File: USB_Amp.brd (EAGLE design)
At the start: 80 x 72 mm, 140 parts, among them CON1 USB-C, CON2 PROG, CON3 DC IN, CON4 VOLUEME, CON5 SWD, IC1 3.3V, IC2 PIC32MZEF, IC3 SSM3582, IC4 +5V, IC5 1.8V, IC6 TL431, IC7 STM32G031F, IC8 +5V, IC9 3.3V, Q1 NPN, Q2 NPN, X1 24.576MHz, X2 22.5792MHz, X3 12MHz

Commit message: 取り合えず
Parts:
- removed CON4: VOLUEME, my_connector:VOL_CON
- removed FB4: FB, my_rcl:1608-J
- removed FB5, FB6, FB7, FB8: FB, my_rcl:2012-FB
- removed JP1: IO, my_connector:1X05
- removed L3, L4: 15uH, my_rcl:L5-7,5
- removed X2: 22.5792MHz, my_rcl:KC3225
- added C65: 0.1u, my_rcl:1005
- added C66, C67: 470u, my_rcl:E5-10
- added C68, C69, C70, C71: 1u, my_rcl:2012
- added C72: 1u, my_rcl:1608C
- added C73, C77, C78, C79, C80: 100p, my_rcl:1608C
- added C74, C75, C76: 4.7u, my_rcl:3216
- added CON6: USB-C, my_connector:5077CR-16-SMC2-BK-TR
- added D6: 1mA, my_rcl:SOD123
- added D7: FAULT, my_rcl:D1608
- added D8: LED2, my_rcl:D1608
- added FB13: FB, my_rcl:3216-FB
- added HT1: HEATSINK-5, my_connector:V2199N1
- added Q3: PNP, my_ic:SC59
- added R27, R34, R35: 1k, my_rcl:1608
- added R28: DNP, my_rcl:1608
- added R29: 1k, my_rcl:2012
- added R30: 100k, my_rcl:1608
- added R31, R32: 5.1k, my_rcl:1608
- added R33, R36, R37: 3.3k, my_rcl:1608
- added R38, R39, R40, R41: 22, my_rcl:1608
- C14, C15: value 22p -> 10p
- C16, C17, C18, C19: value 0.22u -> 1u
- C20: value 10n -> 2.2u; device my_rcl:1005 -> my_rcl:1608C
- C21: value 10n -> 1u; device my_rcl:1005 -> my_rcl:2012
- C22, C23: value 0.1u -> 1u; device my_rcl:1608C -> my_rcl:2012
- C24, C25: device my_rcl:1005 -> my_rcl:3225-3
- C26, C40: value 10u -> 0.1u; device my_rcl:2012 -> my_rcl:3225-3
- C27: value 10u -> 0.47uF; device my_rcl:2012 -> my_rcl:C050W
- C29, C44: value 100p -> 0.47uF; device my_rcl:1608-2 -> my_rcl:C050W
- C31: value 0.1u -> 100p; device my_rcl:1608C -> my_rcl:1608-2
- C34: value 0.1u -> 10n; device my_rcl:C050W -> my_rcl:1005
- C35: value 0.1u -> 100p; device my_rcl:C050W -> my_rcl:1608-2
- C36, C37, C51: value 0.47uF -> 100p; device my_rcl:C050W -> my_rcl:1608-2
- C38: value 47u -> DNP; device my_rcl:E2.5-5 -> my_rcl:1608C
- C39: value 0.1u -> 10u; device my_rcl:1608C -> my_rcl:3216
- C41, C55: value DNP -> 10n; device my_rcl:1608-2 -> my_rcl:1005
- C42: value DNP -> 0.1u; device my_rcl:1608-2 -> my_rcl:1608C
- C45, C46: value 100p -> 0.1u; device my_rcl:1608-2 -> my_rcl:1608C
- C47: value 100p -> 10n; device my_rcl:1608-2 -> my_rcl:1005
- C48: device my_rcl:C050W -> my_rcl:1608C
- C49: value 0.1u -> 1u; device my_rcl:C050W -> my_rcl:1608C
- C50: value 0.47uF -> 0.1u; device my_rcl:C050W -> my_rcl:1608C
- C54: value DNP -> 10u; device my_rcl:1608-2 -> my_rcl:3216
- C56: value 1000u -> 470u; device my_rcl:E5-13 -> my_rcl:E5-10
- C59: value DNP -> 0.47uF; device my_rcl:1608C -> my_rcl:C050W
- C62: value 220u -> 1u; device my_rcl:E2,5-8 -> my_rcl:1608C
- C7: value 22u -> 1u; device my_rcl:3225 -> my_rcl:1608C
- CON3: value DC IN -> PWR IN
- D1: value SBD -> D; device my_rcl:SOD523 -> my_rcl:SOD323
- D4: value 5.6mA -> D; device my_rcl:SOD123 -> my_rcl:SOD323
- FB1, FB2: device my_rcl:1608-J -> my_rcl:1608-FB
- FB3: device my_rcl:1608-J -> my_rcl:2012-R
- IC3: value SSM3582 -> TAS6422; device my_ic:QFN40HT -> my_ic:HSSOP56-F
- IC4: value +5V -> 3.3V; device my_ic:TO220-SOP-DUAL -> my_ic:SOT23-5
- IC5: value 1.8V -> 3.3V
- IC6: device my_ic:SOT89 -> my_ic:TO220-SOP-DUAL
- IC7: value STM32G031F -> STM32G030F
- IC8: value +5V -> 7805
- IC9: value 3.3V -> CH221; device my_ic:SOT23-5 -> my_ic:SOT23-6
- L1, L2: value 15uH -> 10uH; device my_rcl:L5-7,5 -> my_rcl:UA8014
- R1: value 10k -> 5.1
- R10, R11, R12: device my_rcl:1608-J -> my_rcl:1005
- R13: value LRCLK -> 10; device my_rcl:1608-J -> my_rcl:3216-3
- R14: value DATA -> 10; device my_rcl:1608-J -> my_rcl:3216-3
- R15: value SCK -> 39; device my_rcl:1608-J -> my_rcl:1608
- R16: value 10 -> 100; device my_rcl:2012 -> my_rcl:1608
- R17: value 10 -> 50k; device my_rcl:2012 -> my_rcl:RK0972
- R19, R20: device my_rcl:2012 -> my_rcl:3216-3
- R23: value 10k -> 3.3k
- R3: value 10k -> 10; device my_rcl:1608 -> my_rcl:2012-R
- R6: value 1k -> 10k
- R7: value 1k -> 3.3k
- R8: value 10k -> 10
- R9: value 10k -> 39
- TP1, TP2: device my_connector:TESTPIN-BIG -> my_connector:TESTPIN-LARGE
- TP3: value R_P -> R_N; device my_connector:TESTPIN-BIG -> my_connector:TESTPIN-LARGE
- TP4: value R_N -> R_P; device my_connector:TESTPIN-BIG -> my_connector:TESTPIN-LARGE
- X3: device my_rcl:KC3225-2 -> my_rcl:KC3225-CRYSTAL
- moved R17 73.1 mm to (90.0, 46.0), flipped to the top
- moved IC5 71.9 mm to (78.8, 36.5)
- moved C59 68.3 mm to (10.0, 24.5), turned to 270 degrees
- moved C30 61.5 mm to (65.5, 34.0), turned to 90 degrees
- moved C48 60.6 mm to (55.5, 21.8), turned to 270 degrees
- moved R16 60.6 mm to (59.2, 55.2)
- moved C46 57.9 mm to (51.2, 18.8)
- moved IC4 57.3 mm to (62.0, 34.0), turned to 90 degrees
- moved C47 55.0 mm to (51.8, 20.2)
- moved TP4 54.3 mm to (3.25, 17.8)
- moved FB3 54.0 mm to (58.0, 26.8), turned to 270 degrees
- moved C50 53.4 mm to (68.5, 49.2), flipped to the bottom, turned to 90 degrees
- moved TP3 52.1 mm to (3.25, 22.2)
- moved C54 51.4 mm to (67.8, 34.5), turned to 90 degrees
- moved C39 50.5 mm to (53.8, 47.5), flipped to the bottom, turned to 90 degrees
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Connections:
- removed net +12V: C20.1, C21.1, C24.1, C25.1, C26.1, C27.1, C52.+, C53.+, C56.+, IC3.14, IC3.15, IC3.16, IC3.17, IC3.34, IC3.35, IC3.36, IC3.37, Q2.3, R18.2, R21.2
- removed net AMP_AVDD: C23.1, C38.+, C40.1, IC3.24, IC4.3, IC4.6
- removed net EN_44.1K: IC2.29, R9.2, X2.1
- removed net EN_48K: IC2.28, R8.2, X1.1
- removed net MCLK: IC2.22, X1.3, X2.3
- removed net STM_IO16: IC7.16, JP1.2
- removed net STM_IO17: IC7.17, JP1.3
- removed net STM_IO20: IC7.20, JP1.4
- new net AMP_FAULT: IC3.26, IC3.27, R33.2
- new net AMP_MUTE: IC3.25, R35.1
- new net AMP_STANBY: IC3.24, R34.1
- new net I2S_MCLK: IC3.12, R9.2
- new net LED2: IC2.45, R37.2
- new net N$25: C26.1, R13.1
- new net N$26: FB2.2, R8.1
- new net N$27: R15.1, R9.1, X1.3
- new net N$28: FB3.1, R3.2
- new net N$29: Q3.2, R16.1
- new net N$32: CON6.B5:CC2, IC9.5, R32.1
- new net N$33: C49.1, IC9.1, R29.1, R30.2
- new net N$34: IC9.6, R30.1
- new net N$35: D7.K, R33.1
- new net N$37: D1.1, D4.2
- new net N$38: D1.2, D6.1, Q3.1
- new net N$39: IC7.16, R35.2
- new net N$42: IC7.17, R34.2
- new net N$44: D8.A, R37.1
- new net N$45: C77.1, R38.1
- new net N$46: C78.2, R39.2
- new net N$47: C79.2, R40.2
- new net N$48: C80.1, R41.1
- new net N$6: C19.2, IC3.31
- new net PIC_MCLK: IC2.58, R15.2
- new net PVDD: C34.1, C39.1, C41.1, C42.1, C45.1, C46.1, C47.1, C52.+, C53.+, C56.+, C66.+, C68.1, C69.1, C70.1, C74.1, C75.1, C76.1, IC3.2, IC3.29, IC3.30, IC3.42, IC3.43, Q2.3, R18.2, R21.2, R3.1
- new net VBAT: C48.1, C55.1, C67.+, C71.1, FB3.2, IC3.3
- new net VINC_+: CON6.A4,B9:VBUS, CON6.B4,A9:VBUS, FB13.1, R29.2
- net +3V3: now also IC5.5, R17.1, R17.4, R28.2; no longer CON4.1, IC9.5, JP1.1
- net +3V3D: now also C6.1; no longer FB2.1
- net +5V: now also C30.1, C54.1, IC4.1, IC4.3, IC5.1, IC5.3; no longer C62.+, FB3.1, IC9.1, IC9.3
- net AMP_DVDD: now also C62.1, C65.1, C72.1, D7.A, FB2.1, IC3.19, IC4.5; no longer C22.1, IC3.28, IC5.5
- net AMP_OUTN_L: now also C19.1, R40.1; no longer C18.1, C41.2, FB5.2, IC3.33
- net AMP_OUTN_R: now also C17.1, IC3.38, L2.3, R38.2; no longer C19.2, C54.2, FB7.2, IC3.18, IC3.19, L3.2
- net AMP_OUTP_L: now also C18.2, IC3.34, L1.4, R41.2; no longer C16.1, C42.1, FB6.1, IC3.38, IC3.39, L2.2
- net AMP_OUTP_R: now also C16.2, IC3.40, L2.2, R39.1; no longer C17.2, C55.1, FB8.1, IC3.12, IC3.13, L4.1
- net EN_DDC: now also IC1.3, R6.1; no longer R1.1, R3.2
- net GND: now also C24.1, C25.1, C27.1, C27.3, C28.2, C29.1, C29.3, C34.2, C35.1, C36.2, C41.2, C44.3, C46.2, C48.2, C50.2, C54.2, C59.1, C59.3, C62.2, C65.2, C66.-, C67.-, C68.2, C69.2, C70.2, C71.2, C72.2, C73.2, C74.2, C75.2, C76.2, C77.2, C78.1, C79.1, C80.2, CON6.A1,B12:GND, CON6.B1,A12:GND, CON6.SHILED1, CON6.SHILED2, CON6.SHILED3, CON6.SHILED4, CON6.SHILED5, CON6.SHILED6, CON6.SHILED7, CON6.SHILED8, D6.2, D8.K, HT1.HT1, HT1.HT2, IC2.HT2, IC3.11, IC3.16, IC3.17, IC3.18, IC3.28, IC3.33, IC3.36, IC3.39, IC3.46, IC6.5, R17.3, R17.6, R31.2, R32.2, R6.2, R7.1; no longer C21.2, C22.2, C23.2, C24.2, C25.2, C27.2, C28.1, C29.2, C34.1, C34.3, C35.2, C35.4, C36.1, C36.3, C37.3, C38.-, C39.2, C41.1, C46.1, C48.1, C48.3, C49.4, C50.1, C50.3, C51.3, C54.1, C59.2, C62.-, CON4.3, D2.K, IC3.10, IC3.2, IC3.21, IC3.25, IC3.26, IC3.27, IC3.29, IC3.3, IC3.30, IC3.9, IC3.HT, IC3.HT1, IC3.HT2, IC3.HT3, IC3.HT4, IC4.5, JP1.5, R3.1, R8.1, R9.1, X2.2
- net I2C_SCL: now also IC3.20; no longer IC3.4
- net I2C_SDA: now also IC3.21; no longer IC3.5
- net I2S_DATA: now also IC3.15; no longer R14.1
- net I2S_LRCLK: now also IC3.14; no longer R13.1
- net I2S_SCK: now also IC3.13; no longer R15.1
- net LED0: now also D2.A, IC7.3; no longer IC2.2, R6.2
- net LED1: now also IC2.46, R36.2; no longer IC2.3, R7.2
- net N$10: now also C20.1, IC3.9; no longer IC3.6, R13.2
- net N$11: now also C21.2, IC3.8; no longer IC3.7, R14.2
- net N$12: now also C21.1, IC3.7; no longer C18.2, IC3.31
- net N$13: now also C22.1, C23.1, IC3.4; no longer C16.2, IC3.40
- net N$14: now also C18.1, IC3.35; no longer IC3.8, R15.2
- net N$15: now also C22.2, IC3.6; no longer C39.1, IC5.4
- net N$17: now also C17.2, IC3.37; no longer C17.1, IC3.11
- net N$18: now also C23.2, IC3.5; no longer C19.1, IC3.20
- net N$19: now also C16.1, IC3.41; no longer C30.1, FB3.2, IC5.1, IC5.3
- net N$20: now also C38.2, IC6.4, R27.1; no longer R21.1, R22.2
- net N$21: now also C24.2, R19.2; no longer C34.2, C34.4, R16.2
- net N$22: now also C40.1, R20.1; no longer C35.1, C35.3, R17.1
- net N$23: now also C38.1, IC6.6, Q3.3; no longer D4.2
- net N$24: now also C25.2, R14.2; no longer C31.1, FB4.2, IC4.1, IC4.4
- net N$3: now also FB1.2, R1.1; no longer CON1.A4,B9:VBUS, CON1.B4,A9:VBUS, FB1.1
- net N$30: now also C39.2, R21.1, R22.2, R27.2; no longer C48.2, C48.4, R19.2
- net N$31: now also CON6.A5:CC1, IC9.4, R31.1; no longer C49.1, C49.3, R20.1
- net N$4: now also C1.1, C2.1, IC1.1; no longer D1.A, IC1.3
- net N$72: now also C73.1, R17.2, R17.5, R28.1; no longer C59.1, CON4.2
- net N$8: now also D2.K, R7.2; no longer D2.A, R6.1
- net N$9: now also R36.1; no longer R7.1
- net PIC_COM1: now also IC2.44, IC7.15; no longer IC2.62, IC7.12
- net PIC_COM2: now also IC2.43, IC7.14; no longer IC2.64, IC7.13
- net PIC_COM3: now also IC2.42, IC7.13; no longer IC2.63, IC7.14
- net SP_OUTN_L: now also C27.2, C27.4, C35.2, C37.2, R19.1; no longer C28.2, C32.2, C36.2, C36.4, FB5.1, R16.1
- net SP_OUTN_R: now also C31.1, C33.1, C59.2, C59.4, L2.4, R13.2, TP3.1; no longer C44.2, C46.2, C50.2, C50.4, FB7.1, L3.1, R19.1, TP4.1
- net SP_OUTP_L: now also C28.1, C36.1, C44.2, C44.4, L1.3, R20.2; no longer C29.1, C33.1, C37.2, C37.4, FB6.2, L2.1, R17.2
- net SP_OUTP_R: now also C29.2, C29.4, C32.2, L2.1, R14.1, TP4.1; no longer C45.1, C47.1, C51.4, FB8.2, L4.2, R20.2, TP3.1
- net USB_VBUS: now also CON1.A4,B9:VBUS, CON1.B4,A9:VBUS, FB1.1; no longer C1.1, C2.1, D1.K, FB1.2, IC1.1
- net V+: now also C50.1, FB13.2, R16.2; no longer FB4.1
- net XVCC: now also R8.2, X1.1; no longer C6.1, FB2.2, X2.4
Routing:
- net +5V: track 97.1 -> 25.6 mm
- net V+: track 68.4 -> 10.0 mm, vias 0 -> 2
- net +12V: track 51.8 -> 0.00 mm, vias 12 -> 0
- net AMP_MUTE: track 0.00 -> 38.6 mm, vias 0 -> 2
- net AMP_STANBY: track 0.00 -> 38.6 mm, vias 0 -> 2
- net VBAT: track 0.00 -> 31.8 mm, vias 0 -> 2
- net PIC_MCLK: track 0.00 -> 26.0 mm
- net +3V3D: track 32.3 -> 58.3 mm, vias 12 -> 9
- net UART_TX: track 26.9 -> 3.77 mm, vias 1 -> 0
- net SP_OUTP_R: track 22.6 -> 0.00 mm, vias 0 -> 2
- net SP_OUTN_R: track 22.5 -> 0.00 mm, vias 0 -> 2
- net SP_OUTP_L: track 22.3 -> 0.00 mm, vias 0 -> 2
- net SP_OUTN_L: track 22.2 -> 0.00 mm, vias 0 -> 2
- net EN_DDC: track 9.84 -> 31.8 mm, vias 0 -> 2
- net STM_IO20: track 21.5 -> 0.00 mm
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- added copper zone on layer 16, net AMP_OUTN_L
- added copper zone on layer 16, net AMP_OUTN_R
- added copper zone on layer 16, net AMP_OUTP_L
- added copper zone on layer 16, net AMP_OUTP_R
- added copper zone on layer 1, net PVDD
- added copper zone on layer 16, net PVDD
- added copper zone on layer 1, net SP_OUTN_L
- added copper zone on layer 16, net SP_OUTN_L
- added copper zone on layer 1, net SP_OUTN_R
- added copper zone on layer 16, net SP_OUTN_R
- added copper zone on layer 1, net SP_OUTP_L
- added copper zone on layer 16, net SP_OUTP_L
- added copper zone on layer 1, net SP_OUTP_R
- added copper zone on layer 16, net SP_OUTP_R
- removed copper zone on layer 1, net +12V
- removed copper zone on layer 16, net +12V
- removed copper zone on layer 15, net +3V3D
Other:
- board size 80 x 72 mm -> 94 x 64 mm
- board text added: "ver5"
- board text removed: "ver2"

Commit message: 2oz
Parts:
- added TP5: G, my_connector:TESTPIN
- CON1, CON6: value USB-C -> USB-C-2OZ; device my_connector:5077CR-16-SMC2-BK-TR -> my_connector:5077CR-16-SMC2-BK-TR-2OZ
- moved TP10 0.50 mm to (88.5, 26.0)
- moved TP9 0.50 mm to (74.0, 29.5), turned to 270 degrees
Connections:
- net GND: now also TP5.1
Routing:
- net GND: track 59.6 -> 62.8 mm, vias 451 -> 723

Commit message: 定電流源強化
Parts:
- removed D1, D4: D, my_rcl:SOD323
- added Q4: PNP, my_ic:SC59
- R38, R39, R40, R41: device my_rcl:1608 -> my_rcl:2012
- moved R16 5.30 mm to (54.0, 54.5), turned to 0 degrees
- moved D6 4.03 mm to (58.0, 59.8), turned to 180 degrees
- moved Q3 1.77 mm to (58.2, 57.0), turned to 90 degrees
- moved C38 1.41 mm to (58.2, 54.2), turned to 0 degrees
- moved Q1 0.25 mm to (58.8, 51.5)
- moved R38 0.25 mm to (27.0, 26.2)
- moved R39 0.25 mm to (27.0, 13.8)
- moved R40 0.25 mm to (27.0, 51.2)
- moved R41 0.25 mm to (27.0, 38.8)
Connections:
- removed net N$37: D1.1, D4.2
- net N$29: now also Q4.1
- net N$38: now also Q4.3; no longer D1.2
- net V+: now also Q4.2; no longer D4.1
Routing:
- net N$23: track 17.9 -> 8.81 mm
- net N$20: track 8.26 -> 11.6 mm
- net N$29: track 1.67 -> 5.03 mm
- net N$37: track 2.07 -> 0.00 mm
- net V+: track 10.0 -> 8.99 mm
- net N$38: track 7.20 -> 8.15 mm
- net GND: vias 723 -> 745

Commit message: 発注
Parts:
- added C81: 4.7u, my_rcl:3216
- DR4: value HOLE-3.2 -> HOLE-3.2C; device my_connector:HOLE_3.2 -> my_connector:HOLE_3.2_CON2
- moved DR2 89.0 mm to (3.00, 61.0)
- moved DR4 87.0 mm to (91.0, 61.0)
- moved Q1 5.26 mm to (53.5, 51.8)
- moved C39 5.00 mm to (58.8, 47.5)
- moved R22 4.01 mm to (57.0, 51.5)
- moved R27 4.01 mm to (59.0, 51.5)
- moved R18 3.75 mm to (54.5, 48.0)
- moved IC8 1.12 mm to (70.0, 37.5)
- moved C1 1.00 mm to (90.2, 8.50)
- moved C10 1.00 mm to (75.5, 6.25)
- moved C11 1.00 mm to (71.8, 9.00)
- moved C12 1.00 mm to (80.2, 8.00)
- moved C13 1.00 mm to (79.5, 14.8)
- moved C14 1.00 mm to (84.0, 10.0)
- moved C15 1.00 mm to (84.0, 15.5)
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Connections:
- net GND: now also C81.2, DR4.T
- net VBAT: now also C81.1
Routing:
- net N$20: track 11.6 -> 4.29 mm
- net VBAT: track 31.8 -> 27.3 mm
- net N$16: track 7.92 -> 4.13 mm
- net N$23: track 8.81 -> 9.95 mm
- net N$30: track 7.07 -> 6.34 mm
- net PVDD: vias 63 -> 62
- net GND: vias 745 -> 775
- added copper zone on layer 16, net VBAT
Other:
- outline, holes or cut-outs redrawn

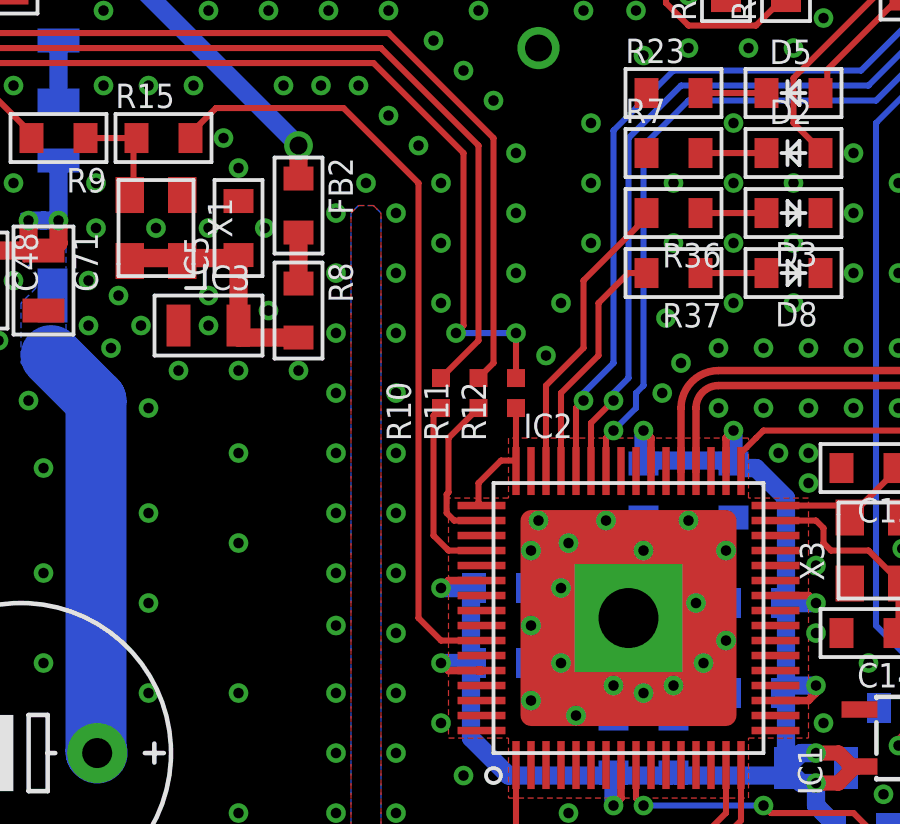
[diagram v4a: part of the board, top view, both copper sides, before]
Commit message: MCLK配線修正
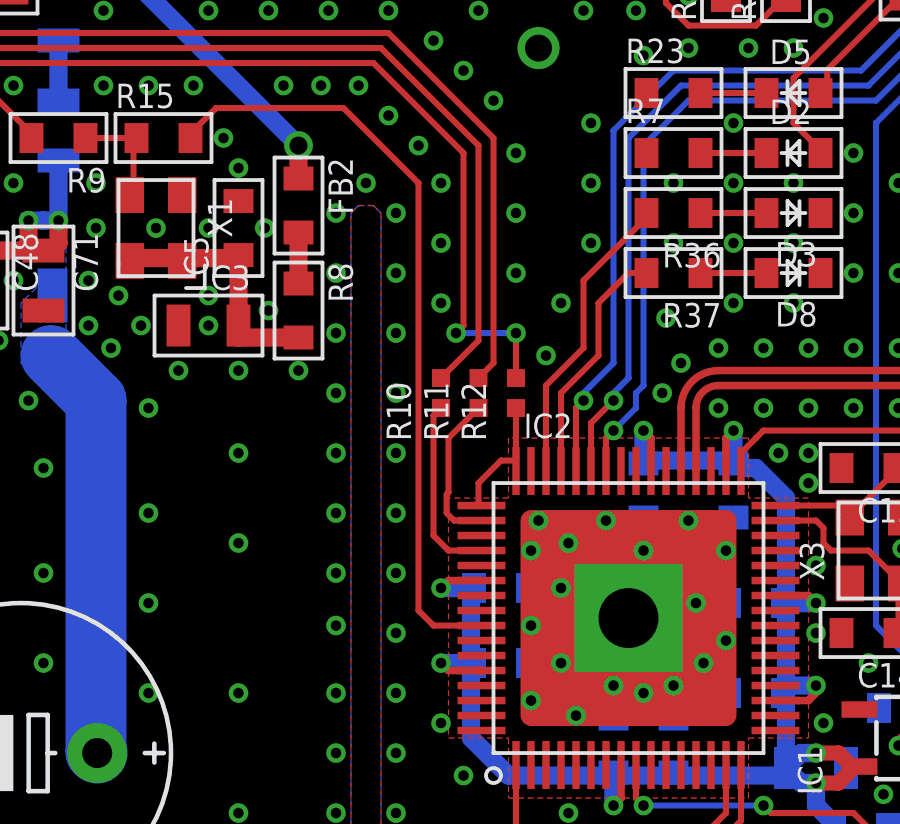
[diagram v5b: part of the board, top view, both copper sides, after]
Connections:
- net PIC_MCLK: now also IC2.57; no longer IC2.58
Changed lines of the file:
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@@
 <signal name="PIC_MCLK">
 <contactref element="R15" pad="2"/>
-<contactref element="IC2" pad="58"/>
-<wire x1="71.1" y1="9.75" x2="69.75" y2="9.75" width="0.2032" layer="1"/>
-<wire x1="69" y1="10.5" x2="69.75" y2="9.75" width="0.2032" layer="1"/>
+<wire x1="69" y1="10.75" x2="69.5" y2="10.25" width="0.2032" layer="1"/>
 <wire x1="61.4" y1="26.5" x2="61.4" y2="26.65" width="0.2032" layer="1"/>
 <wire x1="62.25" y1="27.5" x2="66.5" y2="27.5" width="0.2032" layer="1"/>
 <wire x1="66.5" y1="27.5" x2="69" y2="25" width="0.2032" layer="1"/>
 <wire x1="61.4" y1="26.65" x2="62.25" y2="27.5" width="0.2032" layer="1"/>
-<wire x1="69" y1="25" x2="69" y2="10.5" width="0.2032" layer="1"/>
+<wire x1="69" y1="25" x2="69" y2="10.75" width="0.2032" layer="1"/>
+<contactref element="IC2" pad="57"/>
+<wire x1="71.1" y1="10.25" x2="69.5" y2="10.25" width="0.2032" layer="1"/>
 </signal>
 <signal name="N$3">

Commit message: ver5.1
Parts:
- added R42: 10k, my_rcl:1608
- added R43: 1.5k, my_rcl:1608
- added TP11, TP6: G, my_connector:TESTPIN
- R18: value 1k -> 360
- R30: value 100k -> 200k
- R38, R39, R40, R41: value 22 -> 10
- moved R39 14.1 mm to (29.2, 27.5)
- moved C78 13.8 mm to (29.0, 31.0)
- moved R40 12.0 mm to (29.2, 39.8)
- moved C79 11.9 mm to (29.0, 36.0)
- moved C77 8.51 mm to (26.5, 31.0), turned to 90 degrees
- moved C80 7.02 mm to (26.5, 35.5), turned to 270 degrees
- moved C24 6.27 mm to (10.2, 49.5), turned to 0 degrees
- moved C25 6.27 mm to (10.2, 15.5), turned to 0 degrees
- moved C26 6.27 mm to (10.2, 24.5), turned to 180 degrees
- moved C40 6.27 mm to (10.2, 40.5), turned to 180 degrees
- moved R24 3.51 mm to (91.2, 44.2), turned to 90 degrees
- moved R28 3.51 mm to (91.2, 47.8), turned to 90 degrees
- moved R38 3.13 mm to (24.5, 29.0), turned to 270 degrees
- moved R34 2.85 mm to (80.8, 40.2)
- moved R35 2.85 mm to (80.8, 42.0)
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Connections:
- net N$10 renamed AMP_GVDD
- net N$11 renamed AMP_AVDD
- net N$12 renamed AMP_AVSS
- net N$13 renamed AMP_AREF
- net N$15 renamed AMP_VCOM
- net N$18 renamed AMP_VREG
- new net V+_ADC: IC7.12, R42.1, R43.1
- net +3V3: now also R17.3, R17.6; no longer R17.1, R17.4
- net GND: now also R17.1, R17.4, R43.2, TP11.1, TP6.1; no longer R17.3, R17.6
- net V+: now also R42.2
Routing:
- net V+_ADC: track 0.00 -> 7.21 mm, vias 0 -> 1
- net +3V3: track 32.6 -> 38.9 mm
- net V+: track 8.90 -> 12.5 mm
- net AMP_MUTE: track 38.4 -> 35.4 mm
- net N$39: track 3.28 -> 5.90 mm
- net VBAT: track 27.3 -> 25.3 mm
- net AMP_FAULT: track 7.37 -> 9.12 mm
- net SWDIO: track 12.4 -> 13.4 mm
- net AMP_STANBY: track 38.8 -> 37.9 mm
- net N$72: track 14.9 -> 14.3 mm
- net SWCLK: track 11.1 -> 10.4 mm
- net N$23: track 9.95 -> 10.5 mm
- net N$35: track 1.70 -> 2.20 mm
- net GND: track 62.8 -> 62.3 mm, vias 775 -> 820
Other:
- board text added: "10.9pF"
- board text added: "15.2pF"
- board text added: "17.9pF"
- board text added: "19.3pF"
- board text added: "ver5.1"
- board text removed: "ver5"

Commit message: 微修正
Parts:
- C16, C17, C18, C19: device my_rcl:1608C -> my_rcl:1608-3
- C24, C25, C26, C40: value 0.1u -> 0.01u; device my_rcl:3225-3 -> my_rcl:3216-3
- R13, R14, R19, R20: device my_rcl:3216-3 -> my_rcl:2012-2
- moved C31 5.01 mm to (7.75, 21.8), flipped to the bottom
- moved C32 5.01 mm to (7.75, 18.2), flipped to the bottom
- moved C35 5.01 mm to (7.75, 46.8), flipped to the bottom
- moved C36 5.01 mm to (7.75, 43.2), flipped to the bottom
- moved R13 4.56 mm to (10.8, 22.5), turned to 0 degrees
- moved R14 4.56 mm to (10.8, 17.5), turned to 180 degrees
- moved R19 4.56 mm to (10.8, 47.5), turned to 180 degrees
- moved R20 4.56 mm to (10.8, 42.5), turned to 0 degrees
- moved C24 4.47 mm to (14.2, 47.5), turned to 90 degrees
- moved C25 4.47 mm to (14.2, 17.5), turned to 270 degrees
- moved C26 4.47 mm to (14.2, 22.5), turned to 270 degrees
- moved C40 4.47 mm to (14.2, 42.5), turned to 90 degrees
- moved C27 0.50 mm to (9.00, 50.0), turned to 0 degrees
- moved C29 0.50 mm to (9.00, 15.0), turned to 0 degrees
- moved C44 0.50 mm to (9.00, 40.0), turned to 0 degrees
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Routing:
- net GND: track 62.3 -> 73.9 mm, vias 820 -> 836
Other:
- board text added: "ver5.2"
- board text removed: "ver5.1"
